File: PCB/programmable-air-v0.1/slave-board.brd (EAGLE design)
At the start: 101.5 x 50.8 mm, 18 parts, among them Q1 600mA/40V, Q2 600mA/40V, Q3 600mA/40V

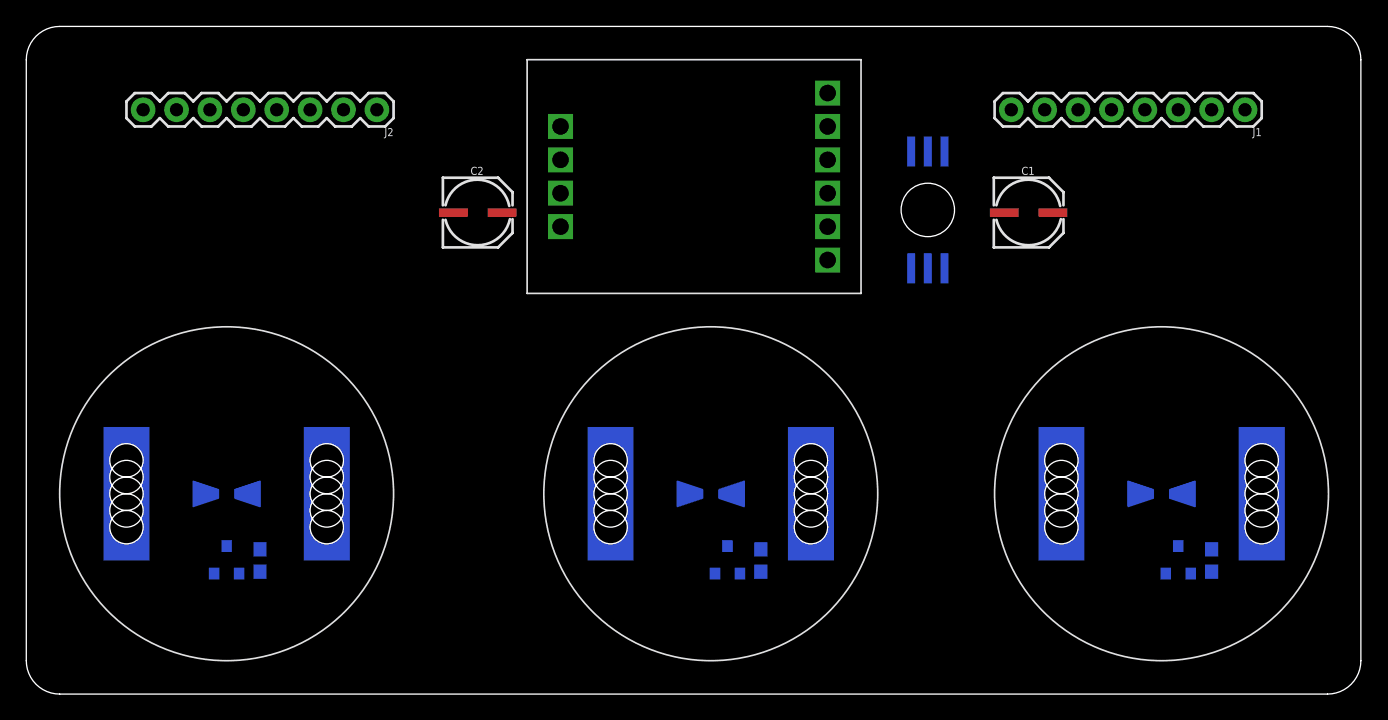
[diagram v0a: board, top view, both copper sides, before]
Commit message: Final tests done. Pump test functional. Workinf on slave board now.
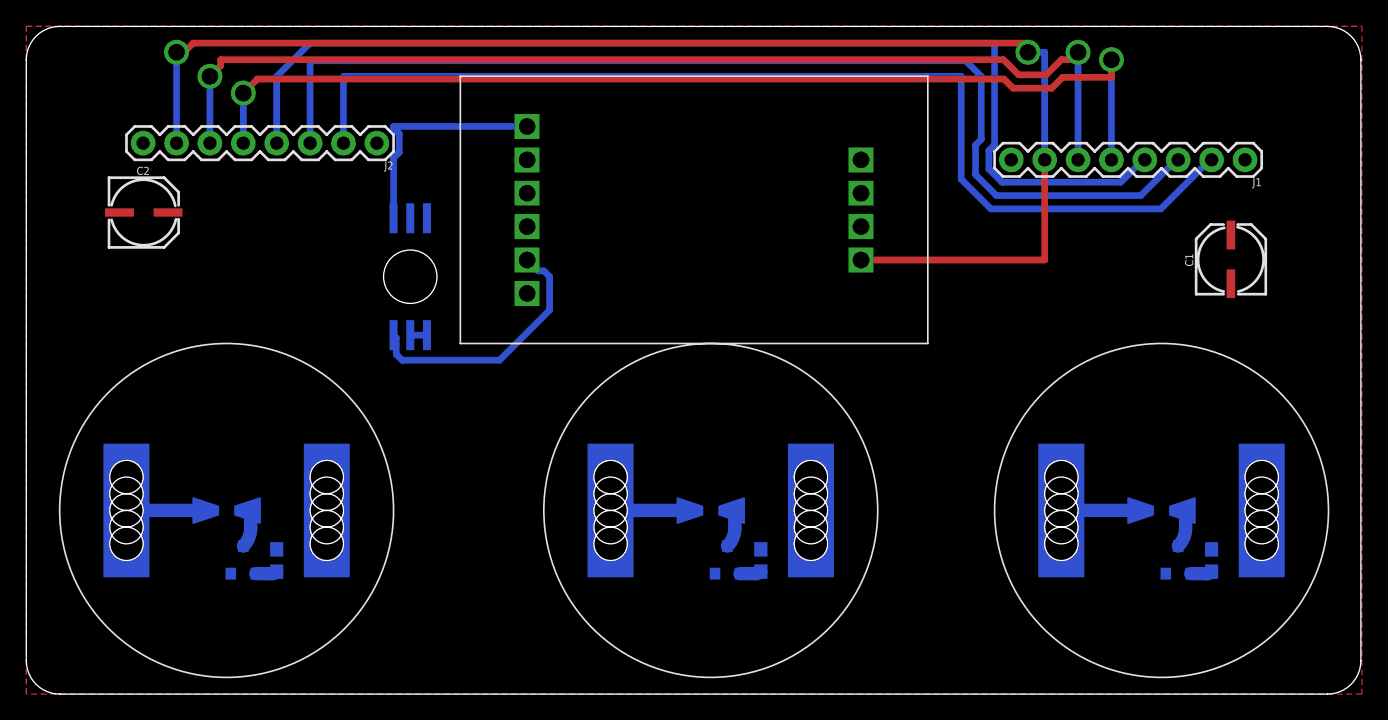
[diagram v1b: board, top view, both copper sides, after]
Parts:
- moved U$8 39.7 mm to (29.2, 31.8)
- moved C2 25.4 mm to (8.89, 36.8)
- moved C1 15.7 mm to (91.4, 33.0), turned to 90 degrees
- moved J1 3.81 mm to (92.7, 40.6)
- moved U$1 3.81 mm to (50.8, 36.8), turned to 0 degrees
- moved J2 2.54 mm to (26.7, 41.9)
- moved Q2 1.27 mm to (16.5, 10.2)
- moved R2 1.27 mm to (19.1, 10.2)
- moved U$2 1.27 mm to (86.4, 14.0)
- moved U$3 1.27 mm to (15.2, 14.0)
- moved U$4 1.27 mm to (52.1, 14.0)
- moved U$5 1.27 mm to (52.1, 14.0)
- moved U$6 1.27 mm to (15.2, 14.0)
- moved U$7 1.27 mm to (86.4, 14.0)
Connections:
- net GND: now also U$1.P$7; no longer U$1.P$8
- net N$11: now also U$1.P$2; no longer U$1.P$7
- net N$14: now also U$1.P$8; no longer U$1.P$5
- net N$16: now also U$1.P$1; no longer U$1.P$6
- net N$4: now also U$1.P$6; no longer U$1.P$3
- net N$6: now also U$1.P$5; no longer U$1.P$4
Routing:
- net N$15: track 0.00 -> 103.7 mm, vias 0 -> 2
- net N$12: track 0.00 -> 83.5 mm
- net N$10: track 0.00 -> 82.6 mm
- net N$14: track 0.00 -> 81.6 mm, vias 0 -> 2
- net N$5: track 0.00 -> 81.4 mm
- net N$13: track 0.00 -> 79.9 mm, vias 0 -> 2
- net N$6: track 0.00 -> 19.8 mm
- net N$16: track 0.00 -> 17.5 mm
- net VIN: track 0.00 -> 17.4 mm
- net N$7: track 0.00 -> 2.82 mm
- net N$9: track 0.00 -> 2.82 mm
- net N$8: track 0.00 -> 2.82 mm
- net N$3: track 0.00 -> 1.62 mm
- net N$1: track 0.00 -> 1.62 mm
- net N$2: track 0.00 -> 1.62 mm
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- added copper zone on layer 1, net GND

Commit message: Slave PCB v0.1 complete
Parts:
- moved U$2 34.3 mm to (52.1, 14.0)
- moved U$4 34.3 mm to (86.4, 14.0)
- moved C2 13.0 mm to (21.6, 34.3)
- moved R1 12.0 mm to (52.1, 21.6)
- moved R2 12.0 mm to (15.2, 21.6)
- moved R3 12.0 mm to (86.4, 21.6)
- moved C1 8.89 mm to (82.5, 33.0), turned to 180 degrees
- moved Q1 7.62 mm to (53.3, 17.8), turned to 180 degrees
- moved Q2 7.62 mm to (16.5, 17.8), turned to 180 degrees
- moved Q3 7.62 mm to (87.6, 17.8), turned to 180 degrees
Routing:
- net VIN: track 17.4 -> 221.9 mm, vias 0 -> 1
- net N$12: track 83.5 -> 142.1 mm, vias 0 -> 2
- net GND: track 0.00 -> 37.9 mm, vias 0 -> 4
- net N$14: track 81.6 -> 117.3 mm, vias 2 -> 3
- net N$10: track 82.6 -> 106.2 mm
- net N$5: track 81.4 -> 101.3 mm
- net N$16: track 17.5 -> 29.9 mm
- net N$13: track 79.9 -> 91.1 mm, vias 2 -> 3
- net N$11: track 1.27 -> 12.2 mm
- net N$4: track 0.00 -> 8.94 mm
- net N$7: track 2.82 -> 8.73 mm
- net N$8: track 2.82 -> 8.73 mm
- net N$9: track 2.82 -> 8.73 mm
- net N$15: track 103.7 -> 107.6 mm
- net N$6: track 19.8 -> 20.4 mm, vias 0 -> 2

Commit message: Modified slave PCB v0.1 based on production and assembly
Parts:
- moved C2 2.84 mm to (19.1, 33.0)
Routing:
- net GND: track 37.9 -> 50.5 mm, vias 4 -> 6
- net N$12: track 142.1 -> 139.6 mm
- net N$15: track 107.6 -> 110.1 mm, vias 2 -> 4
- net VIN: track 221.9 -> 224.3 mm
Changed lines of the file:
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@@
 <attribute name="PROD_ID" value="CAP-08618" x="82.55" y="33.02" size="1.778" layer="27" rot="R180" display="off"/>
 </element>
-<element name="C2" library="SparkFun-Capacitors" package="PANASONIC_C" value="22uF" x="21.59" y="34.29">
-<attribute name="PROD_ID" value="CAP-08618" x="21.59" y="34.29" size="1.778" layer="27" display="off"/>
+<element name="C2" library="SparkFun-Capacitors" package="PANASONIC_C" value="22uF" x="19.05" y="33.02">
+<attribute name="PROD_ID" value="CAP-08618" x="19.05" y="33.02" size="1.778" layer="27" display="off"/>
 </element>
 <element name="J1" library="SparkFun-Connectors" package="1X08" value="" x="92.71" y="40.64" rot="R180">
@@
 <wire x1="73.66" y1="49.52" x2="73.66" y2="41.7767125" width="0.508" layer="16"/>
 <wire x1="21.58" y1="49.52" x2="73.66" y2="49.52" width="0.508" layer="16"/>
-<wire x1="85.09" y1="40.64" x2="85.09" y2="43.18" width="0.508" layer="16"/>
 <via x="19.05" y="44.45" extent="1-16" drill="1.27"/>
 <wire x1="50.8" y1="45.72" x2="52.07" y2="44.45" width="0.508" layer="1"/>
@@
 <via x="82.55" y="46.99" extent="1-16" drill="1.27"/>
 <wire x1="82.55" y1="46.99" x2="82.55" y2="40.64" width="0.508" layer="16"/>
-<wire x1="17.5795" y1="46.7895" x2="66.04" y2="46.7895" width="0.508" layer="1"/>
-<wire x1="66.04" y1="46.7895" x2="74.37048125" y2="46.7895" width="0.508" layer="1"/>
-<wire x1="63.5" y1="35.56" x2="66.04" y2="35.56" width="0.508" layer="16"/>
-<via x="66.04" y="35.56" extent="1-16" drill="1.27"/>
-<wire x1="66.04" y1="35.56" x2="66.04" y2="46.7895" width="0.508" layer="1"/>
+<wire x1="17.5795" y1="46.7895" x2="60.96" y2="46.7895" width="0.508" layer="1"/>
+<wire x1="60.96" y1="46.7895" x2="74.37048125" y2="46.7895" width="0.508" layer="1"/>
+<wire x1="63.5" y1="35.56" x2="60.96" y2="35.56" width="0.508" layer="16"/>
+<via x="60.96" y="35.56" extent="1-16" drill="1.27"/>
+<wire x1="60.96" y1="35.56" x2="60.96" y2="46.7895" width="0.6096" layer="1"/>
 </signal>
 <signal name="N$14">
@@
 <wire x1="68.58" y1="40.64" x2="66.04" y2="38.1" width="0.508" layer="16"/>
 <wire x1="66.04" y1="38.1" x2="63.5" y2="38.1" width="0.508" layer="16"/>
-<wire x1="83.82" y1="44.45" x2="68.58" y2="44.45" width="0.508" layer="1"/>
 <wire x1="13.97" y1="46.99" x2="15.24" y2="48.26" width="0.508" layer="1"/>
 <wire x1="15.24" y1="48.26" x2="74.336825" y2="48.26" width="0.508" layer="1"/>
+<wire x1="83.82" y1="44.45" x2="78.23851875" y2="44.45" width="0.6096" layer="1"/>
+<wire x1="78.23851875" y1="44.45" x2="78.06706875" y2="44.62145" width="0.6096" layer="1"/>
+<wire x1="74.40278125" y1="44.45" x2="68.58" y2="44.45" width="0.6096" layer="1"/>
+<wire x1="78.06706875" y1="44.62145" x2="74.57423125" y2="44.62145" width="0.6096" layer="1"/>
+<wire x1="74.57423125" y1="44.62145" x2="74.40278125" y2="44.45" width="0.6096" layer="1"/>
 </signal>
 <signal name="N$15">
@@
 <via x="76.2" y="48.8215" extent="1-16" drill="1.27"/>
 <wire x1="76.2" y1="48.8215" x2="77.47" y2="48.8215" width="0.508" layer="16"/>
-<wire x1="77.47" y1="48.8215" x2="77.47" y2="40.64" width="0.508" layer="16"/>
+<wire x1="77.47" y1="48.8215" x2="77.47" y2="43.18" width="0.508" layer="16"/>
 <wire x1="11.43" y1="48.8215" x2="12.0015" y2="48.8215" width="0.508" layer="1"/>
 <wire x1="12.0015" y1="48.8215" x2="12.7" y2="49.52" width="0.508" layer="1"/>
 <wire x1="12.7" y1="49.52" x2="76.2" y2="49.52" width="0.508" layer="1"/>
 <wire x1="76.2" y1="49.52" x2="76.2" y2="48.8215" width="0.508" layer="1"/>
-<wire x1="63.5" y1="33.02" x2="77.47" y2="33.02" width="0.508" layer="1"/>
+<wire x1="66.04" y1="33.02" x2="77.47" y2="33.02" width="0.508" layer="1"/>
 <wire x1="77.47" y1="33.02" x2="77.47" y2="40.64" width="0.508" layer="1"/>
 <wire x1="77.47" y1="40.64" x2="77.47" y2="40.005" width="0.6096" layer="16"/>
 <wire x1="80.65" y1="33.22" x2="77.67" y2="33.22" width="0.6096" layer="1"/>
 <wire x1="77.67" y1="33.22" x2="77.47" y2="33.02" width="0.6096" layer="1"/>
+<via x="66.04" y="33.02" extent="1-16" drill="1.27"/>
+<via x="77.47" y="43.18" extent="1-16" drill="1.27"/>
+<wire x1="66.04" y1="33.02" x2="63.5" y2="33.02" width="0.6096" layer="16"/>
+<wire x1="77.47" y1="40.64" x2="77.47" y2="43.18" width="0.6096" layer="16"/>
+<wire x1="77.47" y1="43.18" x2="77.47" y2="40.64" width="0.6096" layer="1"/>
 </signal>
 <signal name="VIN">
@@
 <via x="25.4" y="36.83" extent="1-16" drill="1.27"/>
 <wire x1="25.4" y1="36.83" x2="23.49" y2="34.92" width="1.016" layer="1"/>
-<wire x1="23.49" y1="34.92" x2="23.49" y2="34.09" width="1.016" layer="1"/>
+<wire x1="23.49" y1="34.92" x2="20.95" y2="32.82" width="1.016" layer="1"/>
 <wire x1="25.4" y1="36.83" x2="25.4" y2="34.046575" width="2.54" layer="16"/>
 <wire x1="25.4" y1="34.046575" x2="24.892" y2="33.538575" width="2.54" layer="16"/>
@@
 <wire x1="63.5" y1="40.64" x2="58.42" y2="40.64" width="1.27" layer="16"/>
 <via x="58.42" y="40.64" extent="1-16" drill="1.27"/>
+<wire x1="8.89" y1="41.91" x2="5.08" y2="41.91" width="0.6096" layer="1"/>
+<via x="5.08" y="41.91" extent="1-16" drill="0.8382"/>
+<wire x1="5.08" y1="41.91" x2="8.89" y2="41.91" width="0.6096" layer="16"/>
+<wire x1="75.05065" y1="40.76065" x2="74.93" y2="40.64" width="0.6096" layer="16"/>
+<wire x1="75.05065" y1="43.05935" x2="75.05065" y2="40.76065" width="0.6096" layer="16"/>
+<via x="75.05065" y="43.05935" extent="1-16" drill="1.27"/>
+<wire x1="75.05065" y1="40.76065" x2="75.05065" y2="43.05935" width="0.6096" layer="1"/>
+<wire x1="74.93" y1="40.64" x2="75.05065" y2="40.76065" width="0.6096" layer="1"/>
 </signal>
 <signal name="N$4">
